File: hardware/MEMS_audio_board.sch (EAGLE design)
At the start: 20 parts, among them J1 SJ-2524-SMT, J2 USBSMD, U1 LMV793MF, U2 MIC5365-3.3YD5

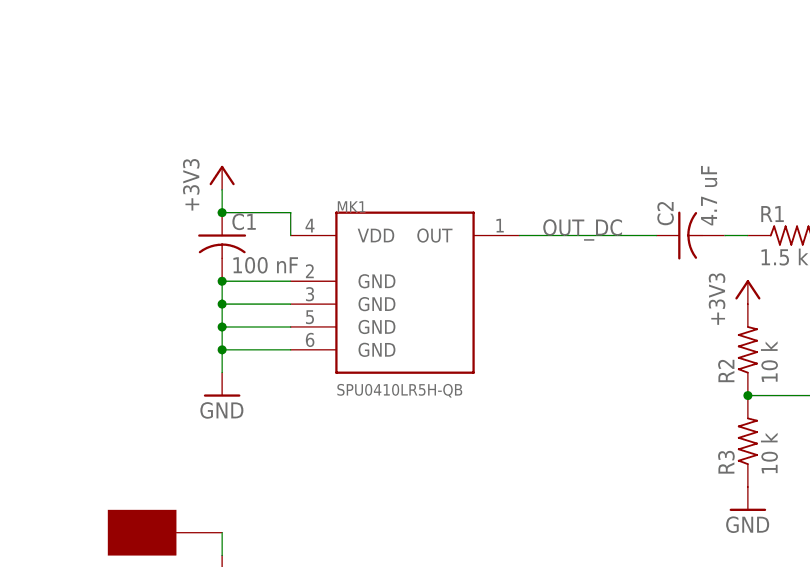
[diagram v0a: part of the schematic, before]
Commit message: corrected flipped mic layout
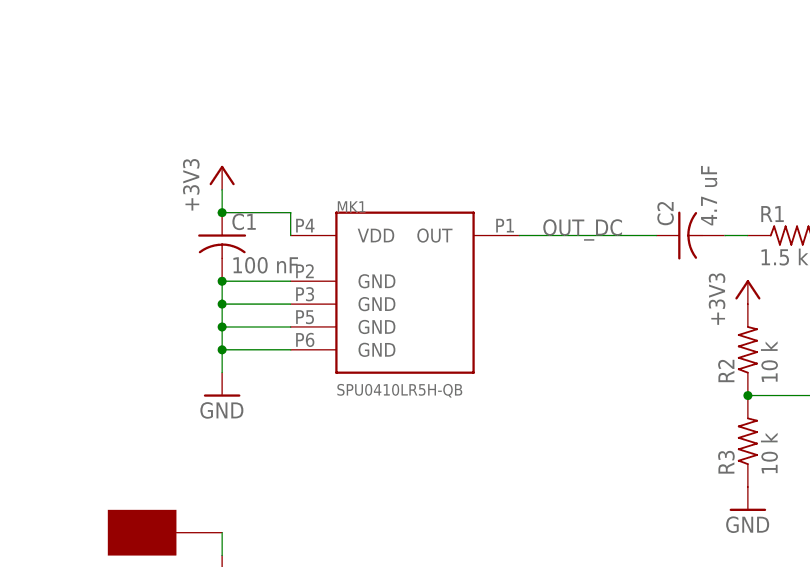
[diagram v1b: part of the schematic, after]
